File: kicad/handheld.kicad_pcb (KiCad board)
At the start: 4 copper layers, 240 x 76 mm, 102 parts, among them J1 Conn_01x08, J2 61300311121, J3 AVR-PDI-6, J4 UE27AC54100, SW1 HOLD, SW10 SELECT, SW2 PAUSE, SW3 SDROP, SW4 HDROP, SW5 ROTR, SW6 RIGHT, SW7 ROTL, SW8 RIGHT, SW9 START, U1 TFBS4711, U10 DMN601, U11 NSI45015, U12 SN54LV574, U13 P-FET, U14 NSI45015, U15 DMN601, U16 NSI45015, U17 NSI45015, U18 DMN601, U19 P-FET, U2 ATxmega64C3-AU, U20 NSI45015, U21 74HCT595, U22 NSI45015, U23 DMN601, U24 NSI45015, U25 P-FET, U26 NSI45015, U27 DMN601, U28 NSI45015, U29 SN54LV574, U3 P-FET, U30 NSI45015, U31 DMN601, U32 NSI45015, U33 P-FET, U34 NSI45015, U35 DMN601, U36 NSI45015, U37 NSI45015, U38 P-FET, U39 DMN601, U4 LM3671MF-3.3, U40 NSI45015, U41 NSI45015, U42 DMN601, U43 NSI45015, U44 SN54LV574, U45 74HCT595, U46 P-FET, U47 NSI45015, U48 DMN601, U49 NSI45015, U5 NSI45015, U50 NSI45015, U51 DMN601, U52 P-FET, U53 NSI45015, U6 P-FET, U7 DMN601, U8 NSI45015, U9 NSI45015

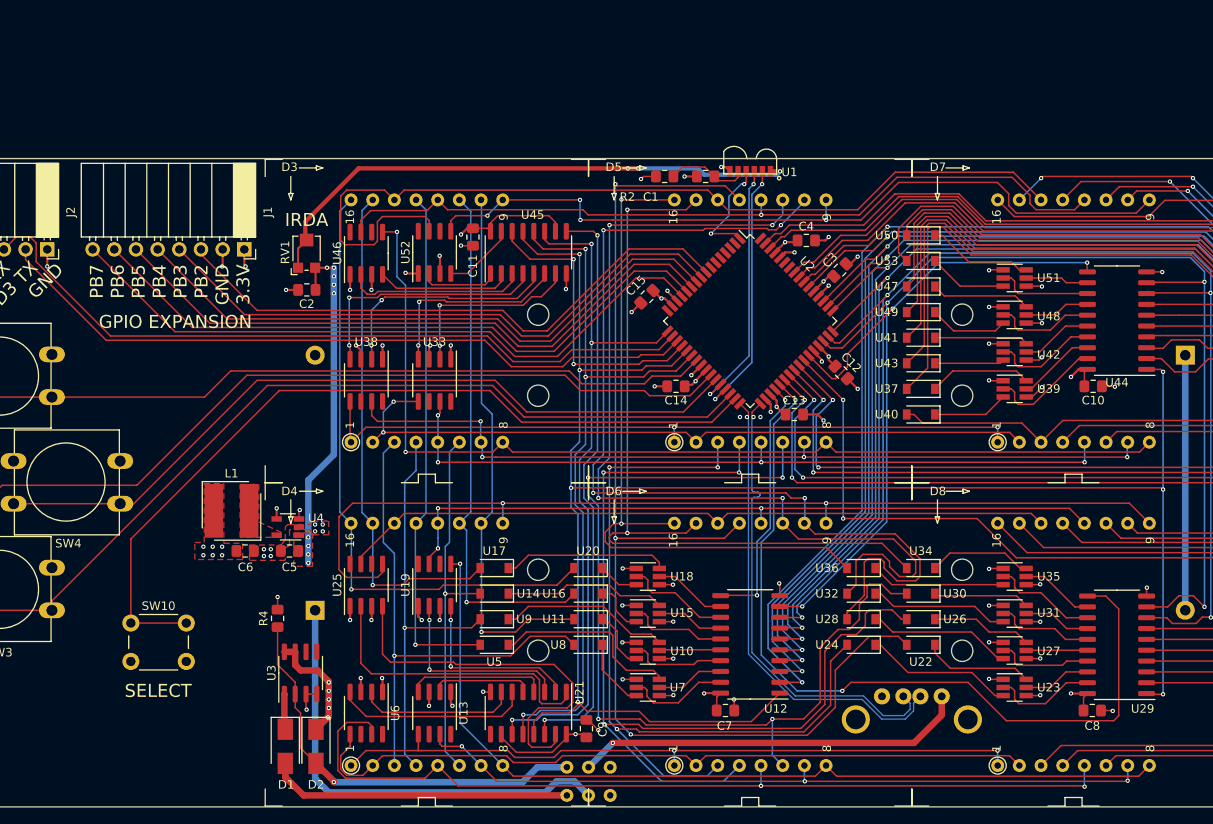
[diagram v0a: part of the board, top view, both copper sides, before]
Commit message: Adding level shifters
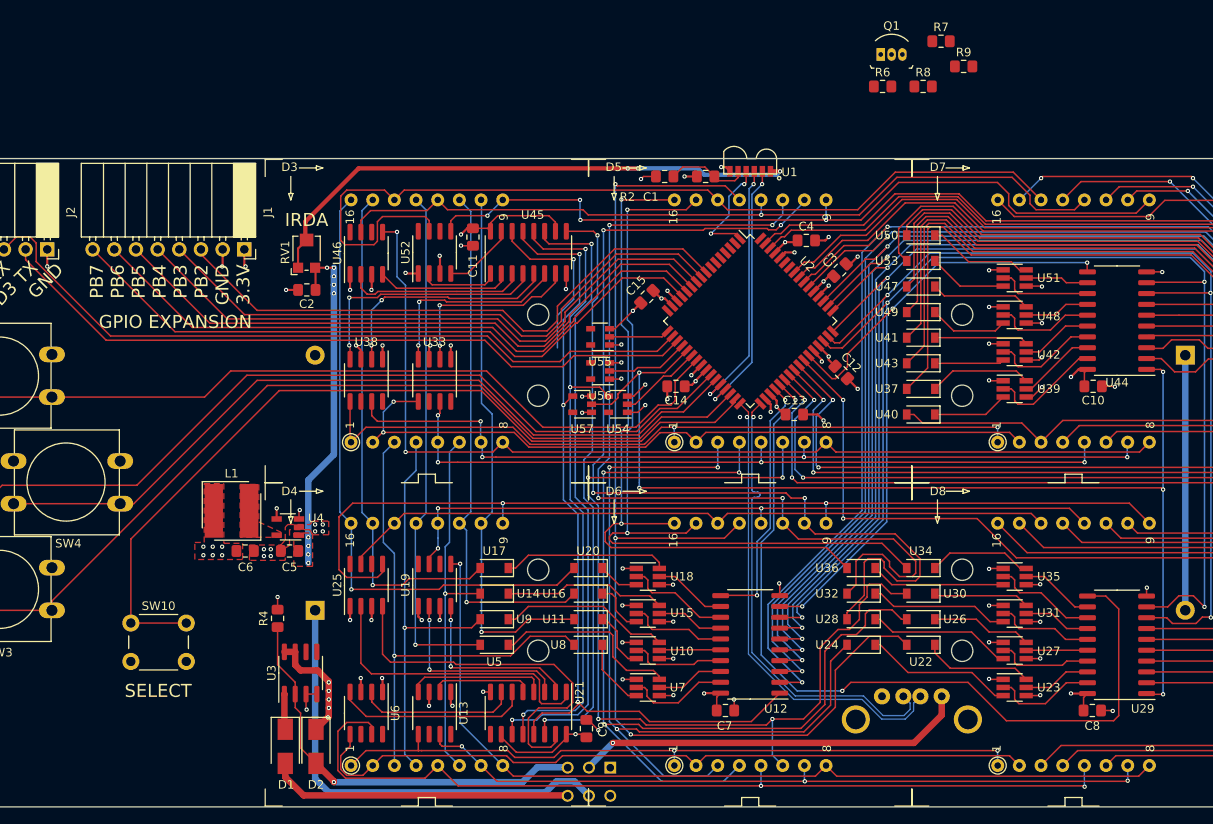
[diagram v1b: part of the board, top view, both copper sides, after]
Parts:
- added Q1: PN2222A, digikey-footprints:TO-92-3, F.Cu at (167.7, 51.4)
- added R6: 5K, Resistor_SMD:R_0805_2012Metric_Pad1.15x1.40mm_HandSolder, F.Cu at (167.9, 55.1)
- added R7: 100R, Resistor_SMD:R_0805_2012Metric_Pad1.15x1.40mm_HandSolder, F.Cu at (174.8, 49.9)
- added R8: 100R, Resistor_SMD:R_0805_2012Metric_Pad1.15x1.40mm_HandSolder, F.Cu at (172.7, 55.1)
- added R9: 100R, Resistor_SMD:R_0805_2012Metric_Pad1.15x1.40mm_HandSolder, F.Cu at (177.4, 52.8)
- added U54: SN74LVC1G08DBVR, Package_TO_SOT_SMD:SOT-23-5, F.Cu at (136.9, 92.4)
- added U55: SN74LVC1G08DBVR, Package_TO_SOT_SMD:SOT-23-5, F.Cu at (134.8, 84.5)
- added U56: SN74LVC1G08DBVR, Package_TO_SOT_SMD:SOT-23-5, F.Cu at (134.8, 88.5)
- added U57: SN74LVC1G08DBVR, Package_TO_SOT_SMD:SOT-23-5, F.Cu at (132.7, 92.4)
- S1: footprint local:JS202011AQN_THT_DPDT -> Button_Switch_THT:SW_CuK_JS202011AQN_DPDT_Angled
- moved S1 3.01 mm to (136.0, 135.0)
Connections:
- BT1 pad 2: /power/BAT_LVL -> Net-(BT1-Pad2)
- BT2 pad 1: /power/BAT_LVL -> Net-(BT1-Pad2)
- S1 pad 2: /power/6V -> /power/5V
- S1 pad 3: Net-(D1-Pad2) -> Net-(D2-Pad2)
- S1 pad 5: /power/5V -> /power/6V
- S1 pad 6: Net-(D2-Pad2) -> Net-(D1-Pad2)
- U12 pad 1: /~OE -> Net-(U21-Pad13)
- U21 pad 11: /ROWCLK -> Net-(U21-Pad11)
- U21 pad 12: /LE -> Net-(U21-Pad12)
- U21 pad 13: /~OE -> Net-(U21-Pad13)
- U45 pad 11: /ROWCLK -> Net-(U21-Pad11)
- U45 pad 12: /LE -> Net-(U21-Pad12)
- U45 pad 13: /~OE -> Net-(U21-Pad13)
- U45 pad 14: /ROWSDI -> Net-(U45-Pad14)
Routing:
- net Net-(U21-Pad13): track 0.00 -> 97.7 mm, vias 0 -> 3
- net /~OE: track 220.2 -> 130.8 mm, vias 7 -> 5
- net Net-(U21-Pad12): track 0.00 -> 76.9 mm, vias 0 -> 3
- net /ROWCLK: track 82.5 -> 7.12 mm, vias 3 -> 0
- net /LE: track 84.9 -> 9.91 mm, vias 3 -> 0
- net Net-(U21-Pad11): track 0.00 -> 73.4 mm, vias 0 -> 2
- net Net-(BT1-Pad2): track 0.00 -> 29.9 mm
- net /power/BAT_LVL: track 29.9 -> 0.00 mm
- net /ROWSDI: track 35.1 -> 9.73 mm, vias 2 -> 0
- net Net-(U45-Pad14): track 0.00 -> 20.4 mm, vias 0 -> 1
- net GND: track 92.9 -> 101.5 mm, vias 65 -> 68
- net VDD: track 38.5 -> 45.0 mm, vias 19 -> 23
- net Net-(SW2-Pad2): track 91.1 -> 96.6 mm
- net Net-(SW1-Pad2): track 106.0 -> 109.5 mm
- net Net-(SW4-Pad1): track 91.4 -> 93.6 mm
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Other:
- board text added: "OFF"
- board text added: "ON"

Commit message: Wired up battery level check
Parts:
- added M3: MountingHole_3.2mm_M3, MountingHole:MountingHole_3.2mm_M3, F.Cu at (47.4, 73.6)
- added M3: MountingHole_3.2mm_M3, MountingHole:MountingHole_3.2mm_M3, F.Cu at (47.4, 129.6)
- added M3: MountingHole_3.2mm_M3, MountingHole:MountingHole_3.2mm_M3, F.Cu at (257.4, 129.6)
- added M3: MountingHole_3.2mm_M3, MountingHole:MountingHole_3.2mm_M3, F.Cu at (257.4, 73.6)
- Q1: footprint digikey-footprints:TO-92-3 -> Package_TO_SOT_THT:TO-92_Inline_W4.0mm_Horizontal_FlatSideDown
- moved R9 89.5 mm to (97.0, 92.2), turned to 180 degrees
- moved R7 86.1 mm to (97.0, 86.7), turned to 180 degrees
- moved Q1 84.3 mm to (91.2, 86.7)
- moved R8 83.1 mm to (97.0, 89.4)
- moved R6 81.3 mm to (97.0, 94.9), turned to 180 degrees
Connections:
- U12 pad 1: Net-(U21-Pad13) -> /~OE
- U2 pad 6: Net-(U2-Pad6) -> /power/BAT_CHK
- U2 pad 64: /power/BAT_LVL -> Net-(U2-Pad64)
- U2 pad 7: Net-(U2-Pad7) -> /power/BAT_LVL
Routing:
- net /power/BAT_CHK: track 0.00 -> 146.4 mm
- net /power/BAT_LVL: track 0.00 -> 141.4 mm
- net /~OE: track 130.8 -> 158.4 mm, vias 5 -> 7
- net Net-(U21-Pad13): track 97.7 -> 72.0 mm
- net U_PWR: track 109.5 -> 130.5 mm, vias 33 -> 38
- net Net-(Q1-Pad2): track 0.00 -> 12.6 mm
- net Net-(U45-Pad14): track 20.4 -> 28.1 mm, vias 1 -> 2
- net Net-(SW2-Pad2): track 96.6 -> 104.0 mm
- net GND: track 101.5 -> 108.5 mm
- net Net-(Q1-Pad1): track 0.00 -> 6.76 mm
- net VDD: track 45.0 -> 48.9 mm, vias 23 -> 22
- net Net-(U45-Pad15): track 8.54 -> 12.3 mm, vias 0 -> 2
- net Net-(SW10-Pad1): track 99.1 -> 102.3 mm
- net Net-(SW3-Pad2): track 108.3 -> 111.3 mm
- net Net-(U21-Pad11): track 73.4 -> 76.2 mm, vias 2 -> 3
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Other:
- outline, holes or cut-outs redrawn

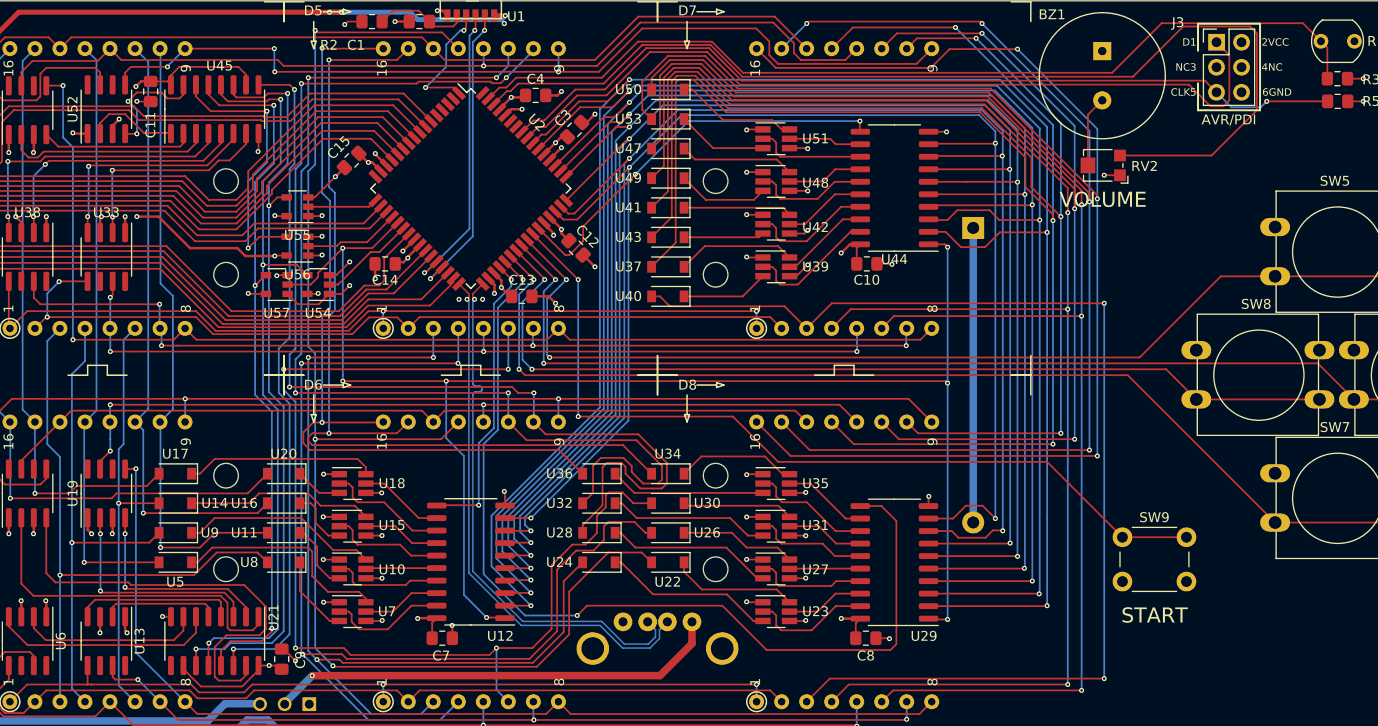
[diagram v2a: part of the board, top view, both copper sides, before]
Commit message: Added mounting holes
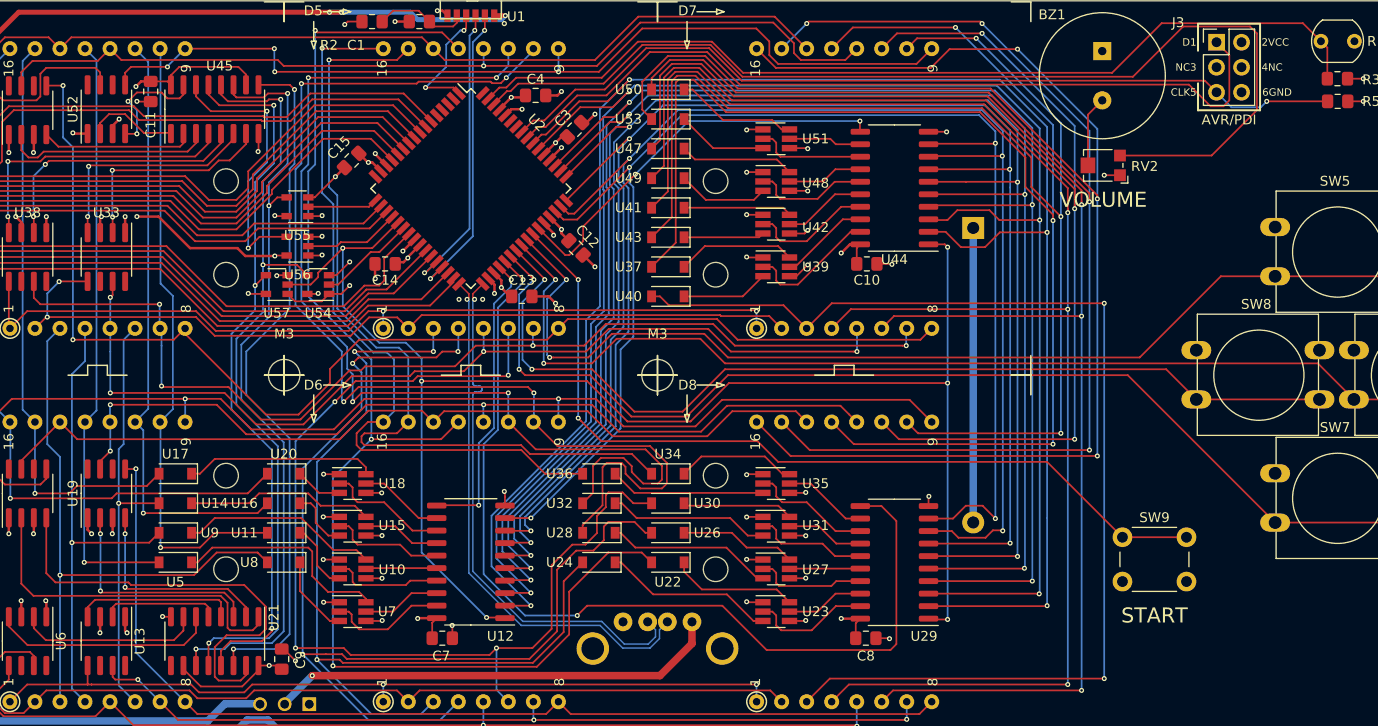
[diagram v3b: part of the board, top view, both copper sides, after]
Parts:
- added M3: MountingHole_3.2mm_M3, MountingHole:MountingHole_3.2mm_M3, F.Cu at (133.4, 101.6)
- added M3: MountingHole_3.2mm_M3, MountingHole:MountingHole_3.2mm_M3, F.Cu at (171.3, 101.6)
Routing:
- net /Matrix Driver/ROW8: track 87.8 -> 98.3 mm
- net /Matrix Driver/ROW6: track 98.1 -> 108.6 mm
- net /Matrix Driver/ROW3: track 117.5 -> 125.7 mm
- net /Matrix Driver/COL14: track 94.3 -> 86.7 mm, vias 2 -> 1
- net /Matrix Driver/COL15: track 84.2 -> 77.0 mm, vias 2 -> 1
- net /Matrix Driver/COL12: track 110.9 -> 105.3 mm
- net /Matrix Driver/ROW9: track 114.2 -> 119.0 mm
- net /Matrix Driver/ROW12: track 85.3 -> 89.9 mm
- net Net-(SW8-Pad2): track 95.8 -> 99.4 mm
- net /Matrix Driver/ROW10: track 84.1 -> 87.6 mm
- net Net-(SW7-Pad2): track 108.8 -> 112.3 mm
- net /Matrix Driver/COL10: track 114.7 -> 111.6 mm
- net Net-(U21-Pad14): track 68.3 -> 71.0 mm
- net /Matrix Driver/COL13: track 111.6 -> 109.0 mm
- net /Matrix Driver/COL9: track 95.7 -> 93.2 mm
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
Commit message: Add silkscreen art and version
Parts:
- added G***: LOGO, arrow:arraw_6mm, F.Cu at (83.2, 105.1)
- added G***: LOGO, arrow:arraw_6mm, F.Cu at (53.6, 85.6)
- added G***: LOGO, arrow:arraw_6mm, F.Cu at (45.4, 98.1)
- added G***: LOGO, arrow:arraw_6mm, F.Cu at (74.9, 117.6)
- added REF**: OSHW-Logo2_7.3x6mm_Copper, Symbol:OSHW-Logo2_7.3x6mm_Copper, F.Cu at (36.1, 89.0)
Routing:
- net Net-(R1-Pad1): track 95.2 -> 96.0 mm
- net /Matrix Driver/ROW16: track 104.6 -> 105.3 mm
- net /IrSD: track 12.9 -> 12.2 mm
- net /Matrix Driver/COL12: track 105.3 -> 104.7 mm
- net Net-(RV2-Pad3): track 107.3 -> 107.9 mm
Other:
- board text added: "A"
- board text added: "B"
- board text added: "Erik van Zijst <erik.van.zijst@gmail.com> https://github.com/erikvanzijst/handheld"
- board text added: "X"
- board text added: "Y"
- board text added: "v0.1 12/2020"

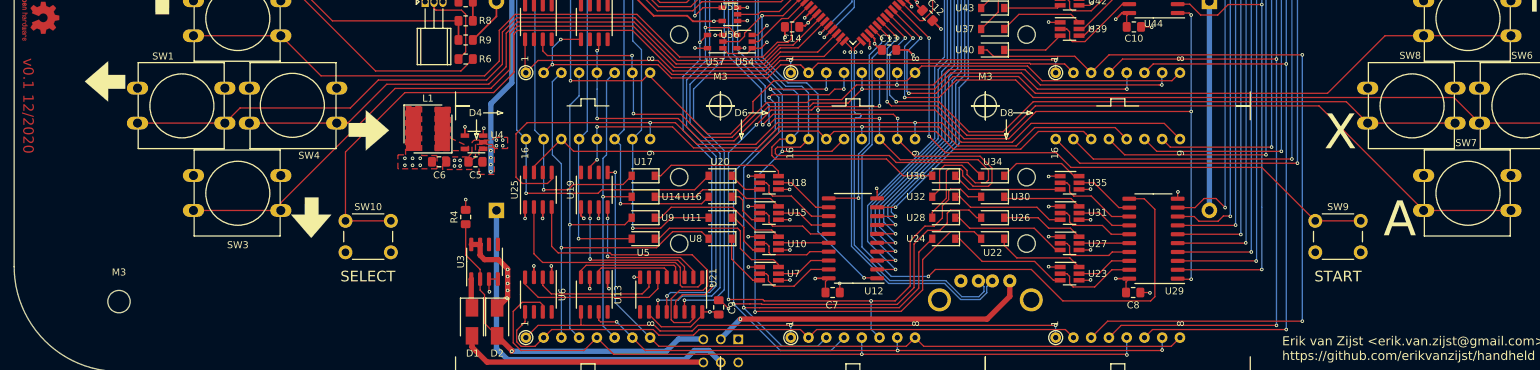
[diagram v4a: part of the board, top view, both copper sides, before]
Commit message: Add logos
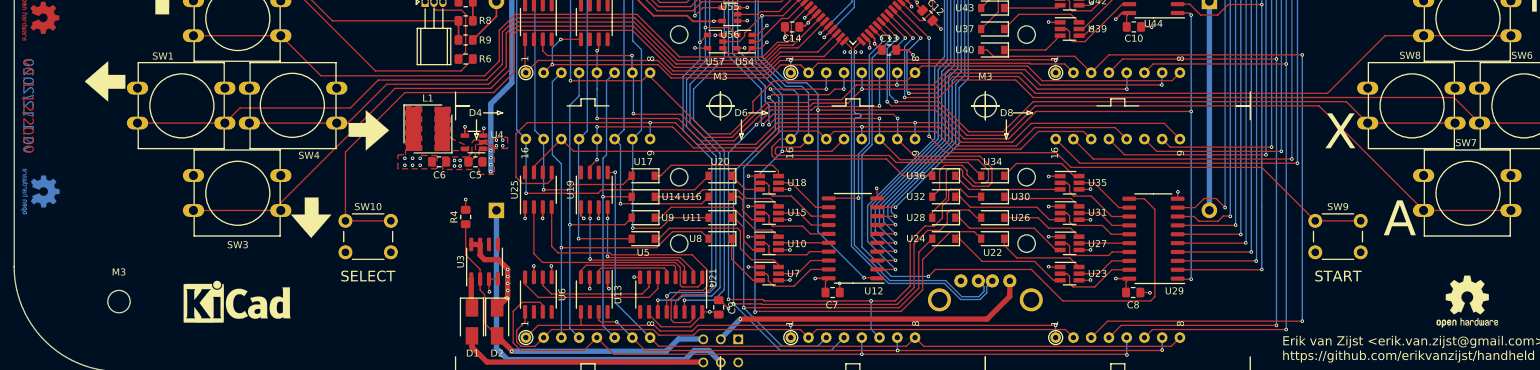
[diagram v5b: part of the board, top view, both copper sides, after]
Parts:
- added REF**: OSHW-Logo2_9.8x8mm_SilkScreen, Symbol:OSHW-Logo2_9.8x8mm_SilkScreen, F.Cu at (240.3, 129.6)
- added REF**: KiCad-Logo_6mm_SilkScreen, Symbol:KiCad-Logo_6mm_SilkScreen, F.Cu at (64.3, 129.6)
- added REF**: OSHW-Logo2_7.3x6mm_Copper, Symbol:OSHW-Logo2_7.3x6mm_Copper, B.Cu at (36.1, 113.8)

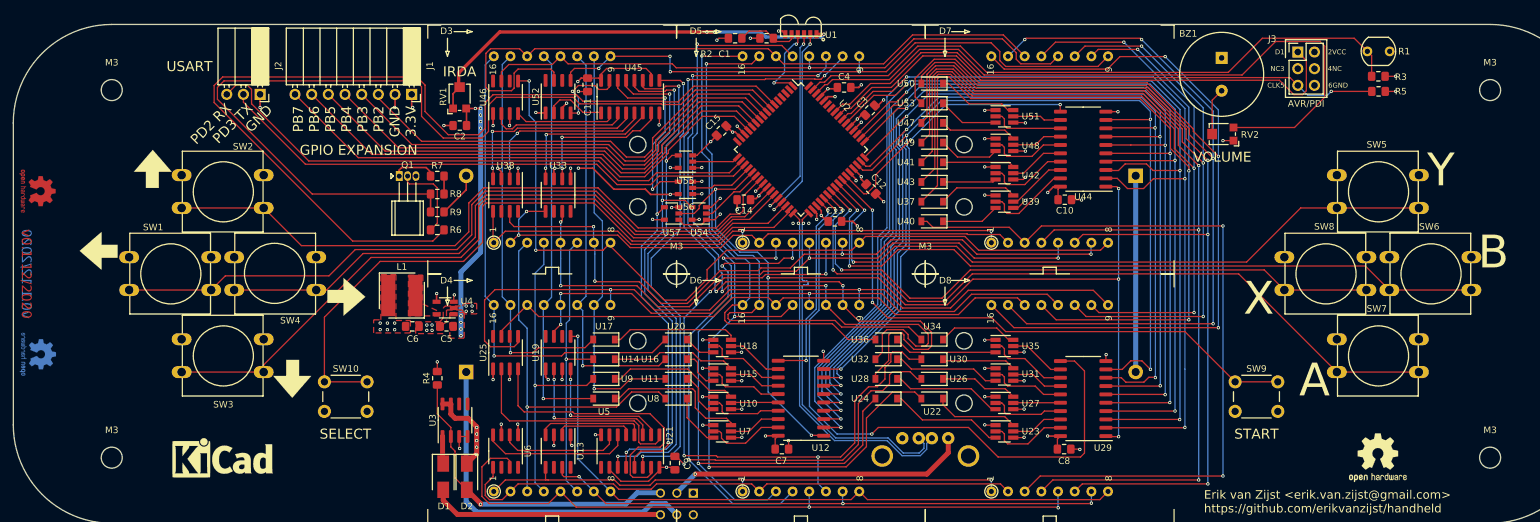
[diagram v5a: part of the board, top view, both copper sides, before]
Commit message: Fix register footprints and add batt indicator
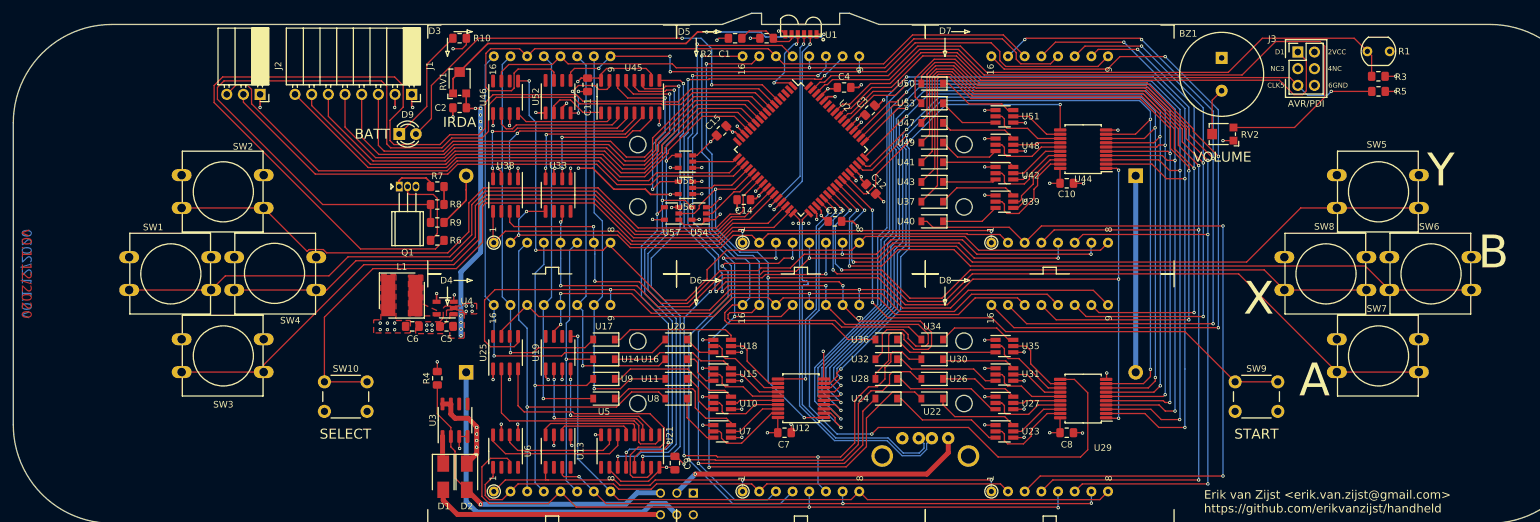
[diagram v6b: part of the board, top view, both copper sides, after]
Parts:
- removed G*** (x4): LOGO, arrow:arraw_6mm
- removed M3 (x6): MountingHole_3.2mm_M3, MountingHole:MountingHole_3.2mm_M3
- removed REF**: OSHW-Logo2_9.8x8mm_SilkScreen, Symbol:OSHW-Logo2_9.8x8mm_SilkScreen
- removed REF**: KiCad-Logo_6mm_SilkScreen, Symbol:KiCad-Logo_6mm_SilkScreen
- removed REF** (x2): OSHW-Logo2_7.3x6mm_Copper, Symbol:OSHW-Logo2_7.3x6mm_Copper
- added D9: BATT LED, LED_THT:LED_D3.0mm, F.Cu at (91.2, 80.3)
- added R10: 150R, Resistor_SMD:R_0805_2012Metric_Pad1.15x1.40mm_HandSolder, F.Cu at (100.4, 65.7)
- R6: value 5K -> 4.7K
- U12, U29, U44: footprint Package_SO:SO-20_5.3x12.6mm_P1.27mm -> Package_SO:SSOP-20_5.3x7.2mm_P0.65mm
- moved C2 2.70 mm to (100.4, 76.3)
- moved C7 2.53 mm to (149.9, 125.8)
- moved C8 2.53 mm to (192.9, 125.8)
- moved C10 2.52 mm to (192.9, 87.8)
- moved RV1 2.30 mm to (100.4, 72.3)
- moved Q1 1.60 mm to (91.2, 88.3)
- moved R6 1.60 mm to (97.0, 96.5)
- moved R7 1.60 mm to (97.0, 88.3)
- moved R8 1.60 mm to (97.0, 91.0)
- moved R9 1.60 mm to (97.0, 93.8)
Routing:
- net Net-(D9-Pad2): track 0.00 -> 71.4 mm, vias 0 -> 2
- net Net-(D9-Pad1): track 0.00 -> 18.0 mm
- net GND: track 108.5 -> 116.1 mm, vias 68 -> 69
- net /power/BAT_CHK: track 146.4 -> 153.1 mm
- net Net-(J1-Pad3): track 69.7 -> 74.8 mm
- net Net-(J1-Pad4): track 71.4 -> 76.1 mm
- net /power/BAT_LVL: track 141.4 -> 145.5 mm
- net Net-(J1-Pad5): track 73.4 -> 77.3 mm
- net Net-(RV1-Pad1): track 67.5 -> 64.5 mm
- net Net-(J1-Pad6): track 75.5 -> 78.4 mm
- net /Matrix Driver/SEGCLK0: track 30.3 -> 33.1 mm
- net /Matrix Driver/SEGCLK2: track 41.4 -> 44.2 mm
- net /D0: track 146.7 -> 149.4 mm
- net Net-(U39-Pad2): track 13.4 -> 15.9 mm
- net /Matrix Driver/SEGCLK1: track 97.1 -> 94.8 mm
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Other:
- board size 240 x 76 mm -> 240 x 77.7 mm
- board text added: "BATT"
- board text added: "RX"
- board text added: "TX"
- board text removed: "PD2 RX"
- board text removed: "PD3 TX"
